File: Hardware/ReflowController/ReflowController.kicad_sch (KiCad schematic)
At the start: 19 parts, among them J101 2060-1452, J102 2060-1452, J103 2060-1453, J104 2060-1452, J105 2060-1452, J106 2060-1452, J107 2060-1452, J108 2060-1452, J109 2060-1452, J110 2060-1452, J111 2060-1452, J112 2060-1452

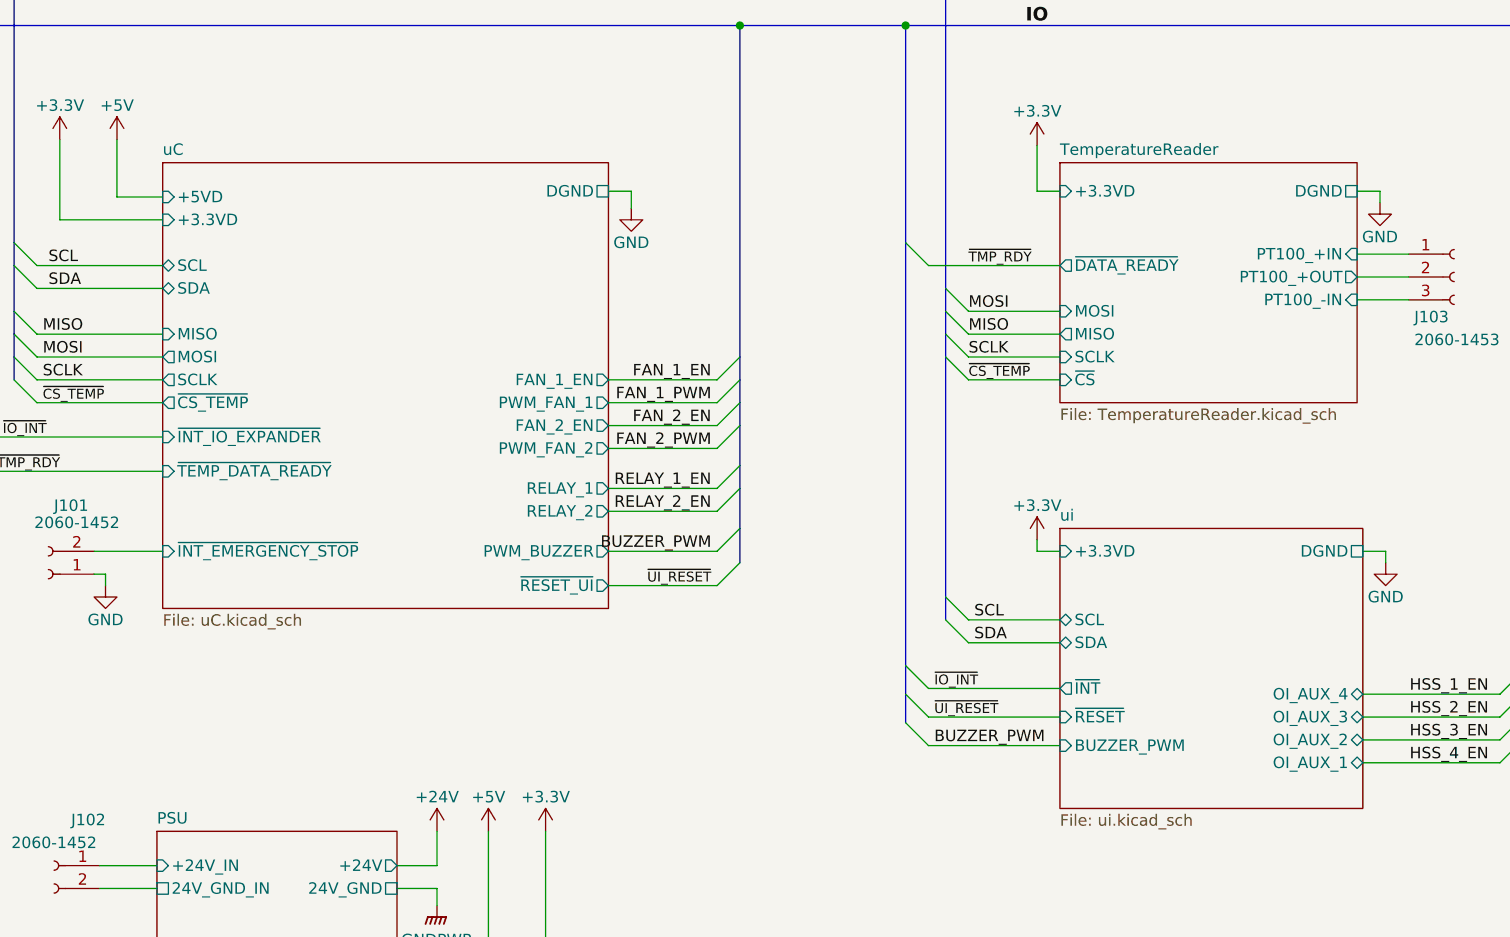
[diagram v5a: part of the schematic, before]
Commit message: changed port table + updated schema
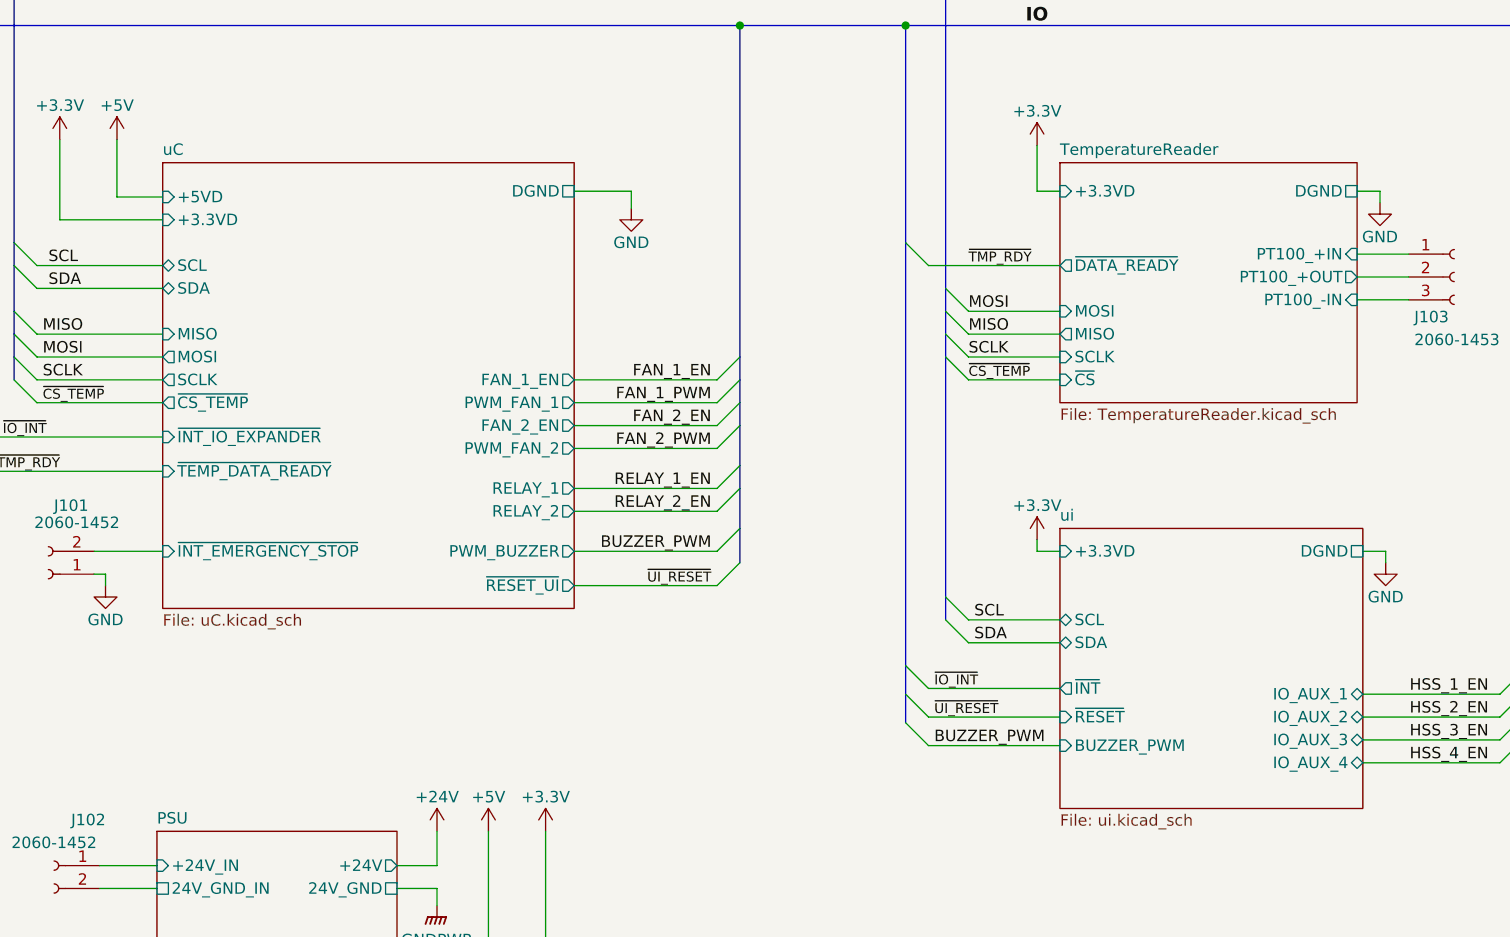
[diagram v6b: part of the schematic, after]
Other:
- sheet ui ports: added IO_AUX_1, IO_AUX_2, IO_AUX_3, IO_AUX_4; removed OI_AUX_1, OI_AUX_2, OI_AUX_3, OI_AUX_4
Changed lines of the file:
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@@
     (stroke (width 0) (type default))
   )
-  (wire (pts (xy 88.9 68.58) (xy 100.965 68.58))
+  (wire (pts (xy 85.09 68.58) (xy 100.965 68.58))
     (stroke (width 0) (type default))
   )
@@
     (stroke (width 0) (type default))
   )
-  (wire (pts (xy 88.9 75.565) (xy 100.965 75.565))
+  (wire (pts (xy 85.09 75.565) (xy 100.965 75.565))
     (stroke (width 0) (type default))
   )
@@
     (stroke (width 0) (type default))
   )
-  (wire (pts (xy 88.9 66.04) (xy 100.965 66.04))
+  (wire (pts (xy 85.09 66.04) (xy 100.965 66.04))
     (stroke (width 0) (type default))
   )
@@
     (stroke (width 0) (type default))
   )
-  (wire (pts (xy 88.9 60.96) (xy 100.965 60.96))
+  (wire (pts (xy 85.09 60.96) (xy 100.965 60.96))
     (stroke (width 0) (type default))
   )
@@
     (stroke (width 0) (type default))
   )
-  (wire (pts (xy 88.9 83.82) (xy 100.965 83.82))
+  (wire (pts (xy 85.09 83.82) (xy 100.965 83.82))
     (stroke (width 0) (type default))
   )
@@
     (stroke (width 0) (type default))
   )
-  (wire (pts (xy 88.9 73.025) (xy 100.965 73.025))
+  (wire (pts (xy 85.09 73.025) (xy 100.965 73.025))
     (stroke (width 0) (type default))
   )
@@
     (stroke (width 0) (type default))
   )
-  (wire (pts (xy 88.9 63.5) (xy 100.965 63.5))
+  (wire (pts (xy 85.09 63.5) (xy 100.965 63.5))
     (stroke (width 0) (type default))
   )
@@
     (stroke (width 0) (type default))
   )
-  (wire (pts (xy 88.9 40.005) (xy 91.44 40.005))
+  (wire (pts (xy 85.09 40.005) (xy 91.44 40.005))
     (stroke (width 0) (type default))
   )
@@
     (stroke (width 0) (type default))
   )
-  (wire (pts (xy 88.9 80.01) (xy 100.965 80.01))
+  (wire (pts (xy 85.09 80.01) (xy 100.965 80.01))
     (stroke (width 0) (type default))
   )
@@
     )
   )
-  (sheet (at 39.37 36.83) (size 49.53 49.53) (fields_autoplaced)
+  (sheet (at 39.37 36.83) (size 45.72 49.53) (fields_autoplaced)
     (stroke (width 0.1524) (type solid))
     (fill (color 0 0 0 0.0000))
@@
       (effects (font (size 1.27 1.27)) (justify left top))
     )
-    (pin "DGND" passive (at 88.9 40.005 0)
+    (pin "DGND" passive (at 85.09 40.005 0)
       (effects (font (size 1.27 1.27)) (justify right))
     )
@@
       (effects (font (size 1.27 1.27)) (justify left))
     )
-    (pin "RELAY_1" output (at 88.9 73.025 0)
-      (effects (font (size 1.27 1.27)) (justify right))
-    )
-    (pin "RELAY_2" output (at 88.9 75.565 0)
-      (effects (font (size 1.27 1.27)) (justify right))
-    )
-    (pin "PWM_BUZZER" output (at 88.9 80.01 0)
-      (effects (font (size 1.27 1.27)) (justify right))
-    )
-    (pin "PWM_FAN_1" output (at 88.9 63.5 0)
-      (effects (font (size 1.27 1.27)) (justify right))
-    )
-    (pin "PWM_FAN_2" output (at 88.9 68.58 0)
+    (pin "RELAY_1" output (at 85.09 73.025 0)
+      (effects (font (size 1.27 1.27)) (justify right))
+    )
+    (pin "RELAY_2" output (at 85.09 75.565 0)
+      (effects (font (size 1.27 1.27)) (justify right))
+    )
+    (pin "PWM_BUZZER" output (at 85.09 80.01 0)
+      (effects (font (size 1.27 1.27)) (justify right))
+    )
+    (pin "PWM_FAN_1" output (at 85.09 63.5 0)
+      (effects (font (size 1.27 1.27)) (justify right))
+    )
+    (pin "PWM_FAN_2" output (at 85.09 68.58 0)
       (effects (font (size 1.27 1.27)) (justify right))
     )
@@
       (effects (font (size 1.27 1.27)) (justify left))
     )
-    (pin "FAN_1_EN" output (at 88.9 60.96 0)
-      (effects (font (size 1.27 1.27)) (justify right))
-    )
-    (pin "FAN_2_EN" output (at 88.9 66.04 0)
+    (pin "FAN_1_EN" output (at 85.09 60.96 0)
+      (effects (font (size 1.27 1.27)) (justify right))
+    )
+    (pin "FAN_2_EN" output (at 85.09 66.04 0)
       (effects (font (size 1.27 1.27)) (justify right))
     )
@@
       (effects (font (size 1.27 1.27)) (justify left))
     )
-    (pin "~{RESET_UI}" output (at 88.9 83.82 0)
+    (pin "~{RESET_UI}" output (at 85.09 83.82 0)
       (effects (font (size 1.27 1.27)) (justify right))
     )
@@
       (effects (font (size 1.27 1.27)) (justify left))
     )
-    (pin "OI_AUX_2" bidirectional (at 172.72 100.965 0)
-      (effects (font (size 1.27 1.27)) (justify right))
-    )
-    (pin "OI_AUX_3" bidirectional (at 172.72 98.425 0)
-      (effects (font (size 1.27 1.27)) (justify right))
-    )
-    (pin "OI_AUX_1" bidirectional (at 172.72 103.505 0)
-      (effects (font (size 1.27 1.27)) (justify right))
-    )
-    (pin "OI_AUX_4" bidirectional (at 172.72 95.885 0)
-      (effects (font (size 1.27 1.27)) (justify right))
-    )
+    (pin "IO_AUX_1" bidirectional (at 172.72 95.885 0)
+      (effects (font (size 1.27 1.27)) (justify right))
+    )
+    (pin "IO_AUX_2" bidirectional (at 172.72 98.425 0)
+      (effects (font (size 1.27 1.27)) (justify right))
+    )
+    (pin "IO_AUX_3" bidirectional (at 172.72 100.965 0)
+      (effects (font (size 1.27 1.27)) (justify right))
+    )
+    (pin "IO_AUX_4" bidirectional (at 172.72 103.505 0)
+      (effects (font (size 1.27 1.27)) (justify right))
+    )

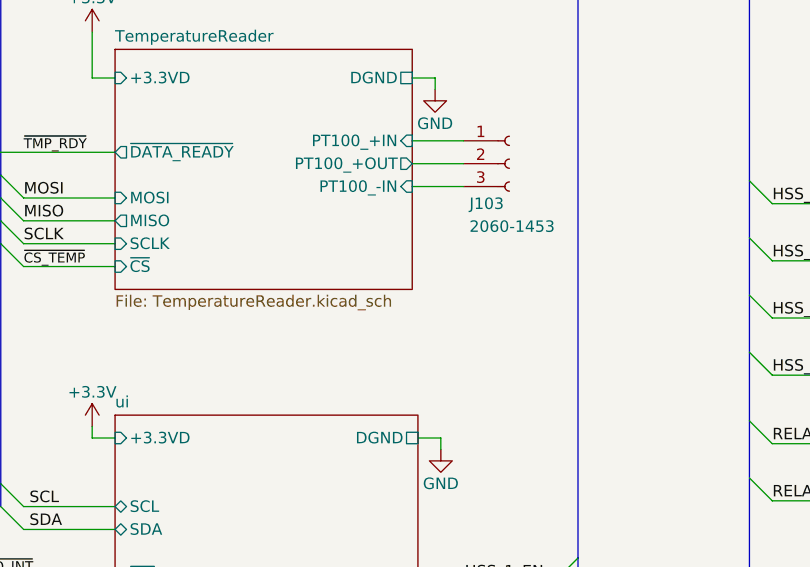
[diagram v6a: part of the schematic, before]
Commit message: work on +24V power
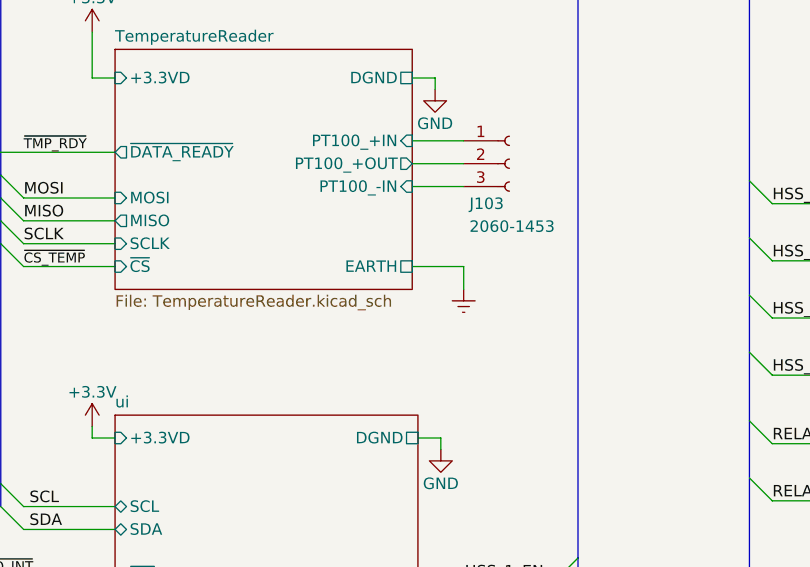
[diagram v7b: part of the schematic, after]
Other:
- sheet TemperatureReader ports: added EARTH; removed none
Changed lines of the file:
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@@
+    (stroke (width 0) (type default))
+  )
+  (wire (pts (xy 177.8 60.96) (xy 177.8 63.5))
     (stroke (width 0) (type default))
   )
@@
   )
   (bus (pts (xy 190.5 100.965) (xy 190.5 102.87))
+    (stroke (width 0) (type default))
+  )
+  (wire (pts (xy 172.085 60.96) (xy 177.8 60.96))
     (stroke (width 0) (type default))
   )
@@
         (path "/2394cc2a-b9b0-4c0b-be11-1fc6085b0d5c"
           (reference "#PWR0114") (unit 1)
+        )
+      )
+    )
+  )
+  (symbol (lib_id "power:Earth") (at 177.8 63.5 0) (unit 1)
+    (in_bom yes) (on_board yes) (dnp no) (fields_autoplaced)
+    (property "Reference" "#PWR01" (at 177.8 69.85 0)
+      (effects (font (size 1.27 1.27)) hide)
+    )
+    (property "Value" "Earth" (at 177.8 67.31 0)
+      (effects (font (size 1.27 1.27)) hide)
+    )
+    (property "Footprint" "" (at 177.8 63.5 0)
+      (effects (font (size 1.27 1.27)) hide)
+    )
+    (property "Datasheet" "~" (at 177.8 63.5 0)
+      (effects (font (size 1.27 1.27)) hide)
+    )
+    (pin "1")
+    (instances
+      (project "ReflowController"
+        (path "/2394cc2a-b9b0-4c0b-be11-1fc6085b0d5c"
+          (reference "#PWR01") (unit 1)
         )
       )
@@
       (effects (font (size 1.27 1.27)) (justify right))
     )
+    (pin "EARTH" passive (at 172.085 60.96 0)
+      (effects (font (size 1.27 1.27)) (justify right))
+    )

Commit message: working on DRC
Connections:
- net Earth: no longer H103.1, H104.1
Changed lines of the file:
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@@
   (junction (at 190.5 21.59) (diameter 0) (color 0 0 0 0)
   )
-  (junction (at 35.56 189.865) (diameter 0) (color 0 0 0 0)
-  )
   (junction (at 36.195 131.445) (diameter 0) (color 0 0 0 0)
   )
   (junction (at 22.86 17.78) (diameter 0) (color 0 0 0 0)
   )
-  (junction (at 40.64 189.865) (diameter 0) (color 0 0 0 0)
-  )
   (junction (at 103.505 21.59) (diameter 0) (color 0 0 0 0)
   )
@@
     (stroke (width 0) (type default))
   )
-  (wire (pts (xy 40.64 189.23) (xy 40.64 189.865))
-    (stroke (width 0) (type default))
-  )
   (bus (pts (xy 209.55 109.855) (xy 209.55 112.395))
     (stroke (width 0) (type default))
@@
     (stroke (width 0) (type default))
   )
-  (wire (pts (xy 40.64 189.865) (xy 52.07 189.865))
-    (stroke (width 0) (type default))
-  )
   (wire (pts (xy 39.37 40.64) (xy 34.29 40.64))
     (stroke (width 0) (type default))
@@
     (stroke (width 0) (type default))
   )
-  (wire (pts (xy 52.07 189.865) (xy 52.07 189.23))
-    (stroke (width 0) (type default))
-  )
   (wire (pts (xy 212.09 80.645) (xy 228.6 80.645))
     (stroke (width 0) (type default))
@@
     (stroke (width 0) (type default))
   )
-  (wire (pts (xy 35.56 189.865) (xy 40.64 189.865))
-    (stroke (width 0) (type default))
-  )
